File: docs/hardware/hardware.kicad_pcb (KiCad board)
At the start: 2 copper layers, 1.4 x 13 mm, 8 parts, among them J1 BASYS_JA, J2 AudioJack2, J6 BASYS_JB, J7 GAMEPAD_1, J8 GAMEPAD_2

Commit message: WIP ppu testing
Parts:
- A1: moved to B.Cu
- moved A1 48.3 mm to (53.3, 66.0)
- moved J7 33.0 mm to (30.5, 20.3)
- moved J8 30.5 mm to (30.5, 53.3)
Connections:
- J1 pad 1: SPI_CLK -> PPU_VRAM_WEN
- J1 pad 3: PPU_VRAM_WEN -> SPI_CLK
- J1 pad 5: (no net) -> GND
- J6 pad 5: unconnected-(J6-Pin_5-Pad5) -> GND
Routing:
- net PPU_VRAM_WEN: track 36.2 -> 26.0 mm
- net SPI_MOSI: track 46.3 -> 36.2 mm
- net SPI_CLK: track 54.0 -> 43.8 mm
- net GND: track 86.9 -> 90.0 mm

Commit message: finalize hardware
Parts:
- added J3: GAMEPAD, Connector_PinHeader_2.54mm:PinHeader_2x04_P2.54mm_Vertical, F.Cu at (119.4, 35.0)
- added SW1: LEFT, Button_Switch_THT:SW_PUSH_6mm, F.Cu at (79.9, 45.7)
- added SW2: UP, Button_Switch_THT:SW_PUSH_6mm, F.Cu at (90.8, 37.1)
- added SW3: RIGHT, Button_Switch_THT:SW_PUSH_6mm, F.Cu at (100.9, 45.7)
- added SW4: PRIMARY, Button_Switch_THT:SW_PUSH_6mm, F.Cu at (137.2, 45.7)
- added SW5: SECONDARY, Button_Switch_THT:SW_PUSH_6mm, F.Cu at (124.5, 45.7)
- added SW6: DOWN, Button_Switch_THT:SW_PUSH_6mm, F.Cu at (90.7, 54.6)
- moved C1 45.8 mm to (99.1, 81.4)
- moved J6 45.8 mm to (83.8, 78.7)
- moved R1 45.8 mm to (91.4, 78.7)
- moved J2 45.8 mm to (109.3, 83.7)
- moved J1 38.9 mm to (38.1, 27.9), turned to -90 degrees
- moved J8 29.0 mm to (58.4, 61.0), turned to 180 degrees
- moved A1 25.4 mm to (27.9, 66.0)
- moved J7 20.5 mm to (50.8, 22.9)
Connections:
- A1 pad 10: GP_P2_DOWN -> GP_P2_BUT_2
- A1 pad 11: GP_P2_LEFT -> GP_P2_BUT_1
- A1 pad 12: GP_P2_RIGHT -> GP_P2_LEFT
- A1 pad 13: GP_P2_BUT_1 -> GP_P2_UP
- A1 pad 14: GP_P2_BUT_2 -> GP_P2_RIGHT
- A1 pad 17: GP_P1_UP -> GP_P1_DOWN
- A1 pad 18: GP_P1_DOWN -> GP_P1_BUT_2
- A1 pad 19: GP_P1_LEFT -> GP_P1_BUT_1
- A1 pad 20: GP_P1_RIGHT -> GP_P1_LEFT
- A1 pad 21: GP_P1_BUT_1 -> GP_P1_UP
- A1 pad 22: GP_P1_BUT_2 -> GP_P1_RIGHT
- A1 pad 9: GP_P2_UP -> GP_P2_DOWN
- J7 pad 1: GP_P1_UP -> GP_P1_LEFT
- J7 pad 2: GP_P1_DOWN -> GP_P1_UP
- J7 pad 3: GP_P1_LEFT -> GP_P1_RIGHT
- J7 pad 5: GP_P1_RIGHT -> GP_P1_BUT_1
- J7 pad 6: GP_P1_BUT_1 -> GP_P1_BUT_2
- J7 pad 7: GP_P1_BUT_2 -> GP_P1_DOWN
- J8 pad 1: GP_P2_UP -> GP_P2_LEFT
- J8 pad 2: GP_P2_DOWN -> GP_P2_UP
- J8 pad 3: GP_P2_LEFT -> GP_P2_RIGHT
- J8 pad 5: GP_P2_RIGHT -> GP_P2_BUT_1
- J8 pad 6: GP_P2_BUT_1 -> GP_P2_BUT_2
- J8 pad 7: GP_P2_BUT_2 -> GP_P2_DOWN
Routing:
- net Net-(J3-VCC): track 0.00 -> 127.5 mm
- net Net-(J3-UP): track 0.00 -> 60.4 mm
- net VCC: track 0.00 -> 58.4 mm
- net GND: track 90.0 -> 49.4 mm, vias 0 -> 1
- net Net-(J3-SECONDARY): track 0.00 -> 39.6 mm
- net Net-(J3-RIGHT): track 0.00 -> 32.5 mm
- net Net-(J3-DOWN): track 0.00 -> 32.2 mm
- net SPI_CLK: track 43.8 -> 13.3 mm, vias 0 -> 1
- net SPI_MOSI: track 36.2 -> 10.8 mm, vias 0 -> 1
- net Net-(J3-PRIMARY): track 0.00 -> 22.0 mm
- net Net-(J3-LEFT): track 0.00 -> 20.1 mm
- net GP_P2_DOWN: track 0.00 -> 15.2 mm
- net GP_P2_RIGHT: track 0.00 -> 15.2 mm
- net GP_P1_RIGHT: track 0.00 -> 15.2 mm
- net GP_P1_DOWN: track 0.00 -> 15.2 mm
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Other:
- board text added: "ARDUINO SHIELD (TOP VIEW)"
- board text added: "GAMEPAD LAYOUT/PINOUT"
- board text added: "PWM AUDIO OUTPUT LOW PASS FILTER"

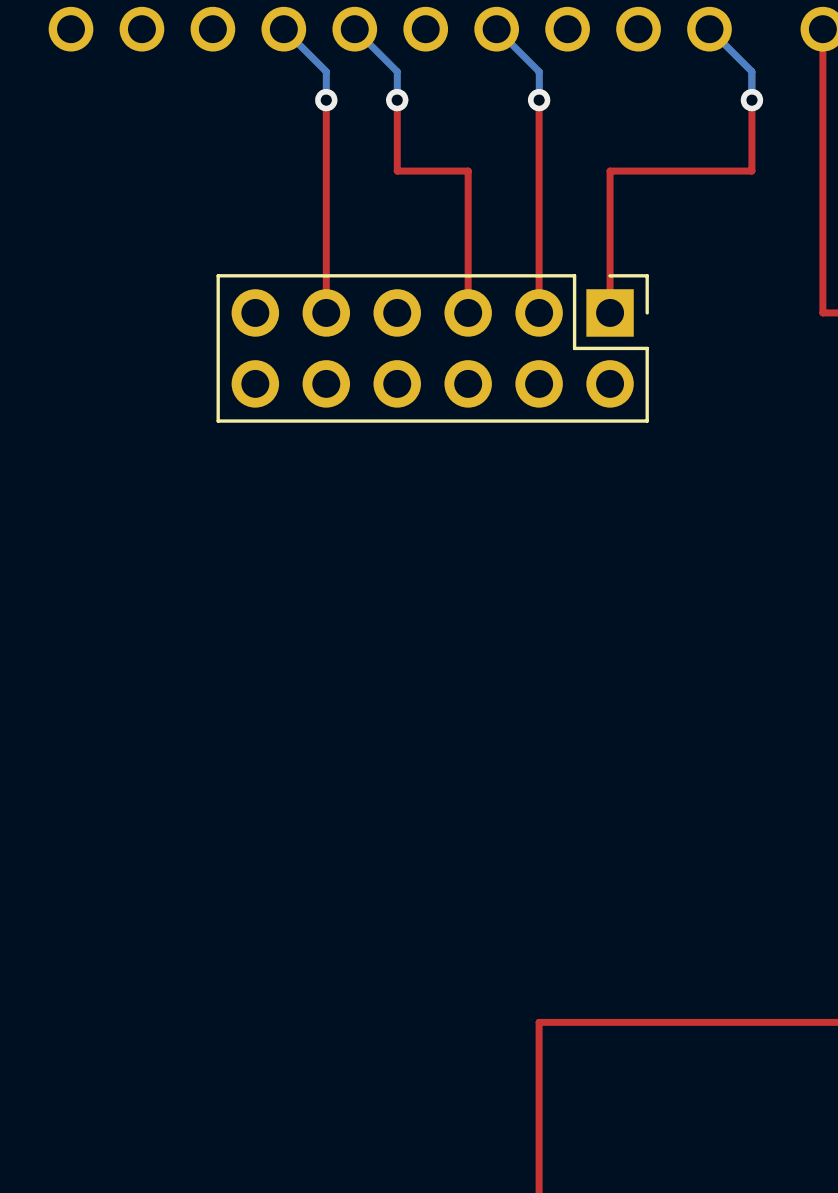
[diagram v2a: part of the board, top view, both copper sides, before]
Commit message: add power source toggle switch to hardware schematics
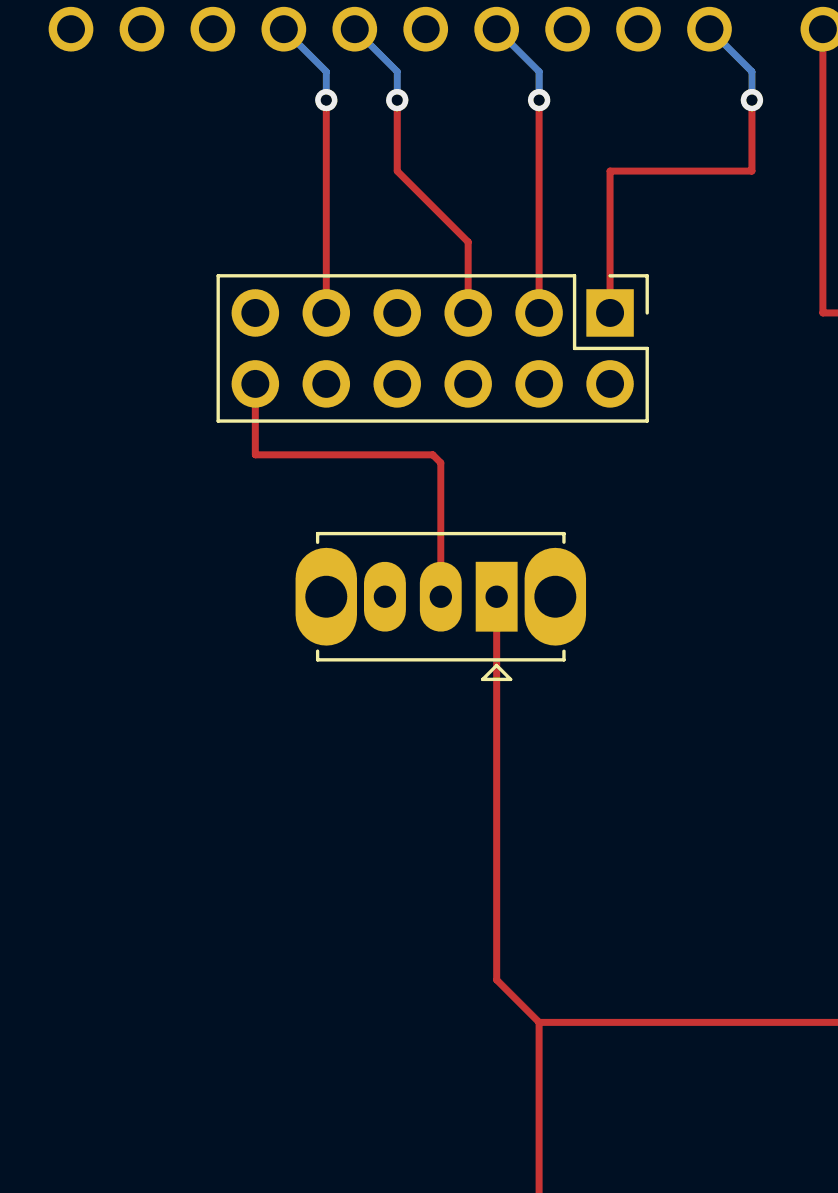
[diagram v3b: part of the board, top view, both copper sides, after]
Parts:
- added SW7: STM_PWR_SOURCE, Button_Switch_THT:SW_Slide_1P2T_CK_OS102011MS2Q, F.Cu at (34.0, 38.1)
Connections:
- J1 pad 12: unconnected-(J1-Pin_12-Pad12) -> Net-(J1-Pin_12)
- J1 pad 6: unconnected-(J1-Pin_6-Pad6) -> Net-(J1-Pin_12)
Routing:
- net VCC: track 58.4 -> 74.3 mm
- net Net-(J1-Pin_12): track 0.00 -> 14.1 mm
- net SPI_CLK: track 13.3 -> 11.8 mm
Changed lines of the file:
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@@
   (net 19 "Net-(C1-Pad1)")
   (net 20 "unconnected-(J1-Pin_4-Pad4)")
-  (net 21 "unconnected-(J1-Pin_6-Pad6)")
+  (net 21 "Net-(J1-Pin_12)")
   (net 22 "unconnected-(J1-Pin_7-Pad7)")
   (net 23 "unconnected-(J1-Pin_8-Pad8)")
   (net 24 "unconnected-(J1-Pin_9-Pad9)")
   (net 25 "unconnected-(J1-Pin_10-Pad10)")
-  (net 26 "unconnected-(J1-Pin_12-Pad12)")
+  (net 26 "unconnected-(SW7-C-Pad3)")
   (net 27 "unconnected-(J6-Pin_1-Pad1)")
   (net 28 "unconnected-(J6-Pin_2-Pad2)")
@@
         (effects (font (size 1 1) (thickness 0.15)))
     )
-    (fp_text value "BASYS_JA" (at 1.27 15.03 90) (layer "F.Fab")
+    (fp_text value "BASYS_JA" (at 1.27 15.03 90) (layer "F.Fab") hide
         (effects (font (size 1 1) (thickness 0.15)))
     )
@@
       (net 6 "GND") (pinfunction "Pin_5") (pintype "passive"))
     (pad "6" thru_hole oval (at 0 12.7 270) (size 1.7 1.7) (drill 1) (layers "*.Cu" "*.Mask")
-      (net 21 "unconnected-(J1-Pin_6-Pad6)") (pinfunction "Pin_6") (pintype "passive"))
+      (net 21 "Net-(J1-Pin_12)") (pinfunction "Pin_6") (pintype "passive"))
     (pad "7" thru_hole oval (at 2.54 0 270) (size 1.7 1.7) (drill 1) (layers "*.Cu" "*.Mask")
       (net 22 "unconnected-(J1-Pin_7-Pad7)") (pinfunction "Pin_7") (pintype "passive"))
@@
       (net 6 "GND") (pinfunction "Pin_11") (pintype "passive"))
     (pad "12" thru_hole oval (at 2.54 12.7 270) (size 1.7 1.7) (drill 1) (layers "*.Cu" "*.Mask")
-      (net 26 "unconnected-(J1-Pin_12-Pad12)") (pinfunction "Pin_12") (pintype "passive"))
+      (net 21 "Net-(J1-Pin_12)") (pinfunction "Pin_12") (pintype "passive"))
     (model "${KICAD6_3DMODEL_DIR}/Connector_PinHeader_2.54mm.3dshapes/PinHeader_2x06_P2.54mm_Vertical.wrl"
       (offset (xyz 0 0 0))
@@
         (effects (font (size 1 1) (thickness 0.15)))
     )
-    (fp_text value "GAMEPAD_2" (at 1.27 9.95) (layer "F.Fab")
-        (effects (font (size 1 1) (thickness 0.15)))
-    )
-    (fp_text user "${REFERENCE}" (at 1.27 3.81 90) (layer "F.Fab")
+    (fp_text value "GAMEPAD_2" (at 1.27 9.95) (layer "F.Fab") hide
         (effects (font (size 1 1) (thickness 0.15)))
     )
@@
       (net 40 "Net-(J3-VCC)") (pinfunction "B") (pintype "passive"))
     (model "${KICAD6_3DMODEL_DIR}/Button_Switch_THT.3dshapes/SW_PUSH_6mm.wrl"
+      (offset (xyz 0 0 0))
+      (scale (xyz 1 1 1))
+      (rotate (xyz 0 0 0))
+    )
+  )
+  (footprint "Button_Switch_THT:SW_Slide_1P2T_CK_OS102011MS2Q" (layer "F.Cu")
+    (at 34.04 38.1 180)
+    (descr "CuK miniature slide switch, OS series, SPDT, https://www.ckswitches.com/media/1428/os.pdf")
+    (tags "switch SPDT")
+    (property "Sheetfile" "hardware.kicad_sch")
+    (property "Sheetname" "")
+    (property "ki_description" "Switch, single pole double throw")
+    (property "ki_keywords" "switch single-pole double-throw spdt ON-ON")
+    (attr through_hole)
+    (fp_text reference "SW7" (at 3.99 -2.99) (layer "F.SilkS") hide
+        (effects (font (size 1 1) (thickness 0.15)))
+    )
+    (fp_text value "STM_PWR_SOURCE" (at 1.779337 -3.676307) (layer "F.Fab") hide
+        (effects (font (size 1 1) (thickness 0.15)))
+    )
+    (fp_line (start -2.41 -2.26) (end 6.41 -2.26)
+      (stroke (width 0.12) (type solid)) (layer "F.SilkS"))
+    (fp_line (start -2.41 -1.95) (end -2.41 -2.26)
+      (stroke (width 0.12) (type solid)) (layer "F.SilkS"))
+    (fp_line (start -2.41 2.26) (end -2.41 1.95)
+      (stroke (width 0.12) (type solid)) (layer "F.SilkS"))
+    (fp_line (start -0.5 -2.96) (end 0 -2.46)
+      (stroke (width 0.12) (type solid)) (layer "F.SilkS"))
+    (fp_line (start 0 -2.46) (end 0.5 -2.96)
+      (stroke (width 0.12) (type solid)) (layer "F.SilkS"))
+    (fp_line (start 0.5 -2.96) (end -0.5 -2.96)
+      (stroke (width 0.12) (type solid)) (layer "F.SilkS"))
+    (fp_line (start 6.41 -2.26) (end 6.41 -1.95)
+      (stroke (width 0.12) (type solid)) (layer "F.SilkS"))
+    (fp_line (start 6.41 2.26) (end -2.41 2.26)
+      (stroke (width 0.12) (type solid)) (layer "F.SilkS"))
+    (fp_line (start 6.41 2.26) (end 6.41 1.95)
+      (stroke (width 0.12) (type solid)) (layer "F.SilkS"))
+    (fp_line (start -3.45 -2.4) (end 7.45 -2.4)
+      (stroke (width 0.05) (type solid)) (layer "B.CrtYd"))
+    (fp_line (start -3.45 2.4) (end -3.45 -2.4)
+      (stroke (width 0.05) (type solid)) (layer "B.CrtYd"))
+    (fp_line (start 7.45 -2.4) (end 7.45 2.4)
+      (stroke (width 0.05) (type solid)) (layer "B.CrtYd"))
+    (fp_line (start 7.45 2.4) (end -3.45 2.4)
+      (stroke (width 0.05) (type solid)) (layer "B.CrtYd"))
+    (fp_line (start -2.3 -2.15) (end -0.5 -2.15)
+      (stroke (width 0.1) (type solid)) (layer "F.Fab"))
+    (fp_line (start -2.3 2.15) (end -2.3 -2.15)
+      (stroke (width 0.1) (type solid)) (layer "F.Fab"))
+    (fp_line (start -0.5 -2.15) (end 0 -1.65)
+      (stroke (width 0.1) (type solid)) (layer "F.Fab"))
+    (fp_line (start 0 -1.65) (end 0.5 -2.15)
+      (stroke (width 0.1) (type solid)) (layer "F.Fab"))
+    (fp_line (start 0 -1) (end 0 1)
+      (stroke (width 0.1) (type solid)) (layer "F.Fab"))
+    (fp_line (start 0 -1) (end 4 -1)
+      (stroke (width 0.1) (type solid)) (layer "F.Fab"))
+    (fp_line (start 0 1) (end 4 1)
+      (stroke (width 0.1) (type solid)) (layer "F.Fab"))
+    (fp_line (start 0.5 -2.15) (end 6.3 -2.15)
+      (stroke (width 0.1) (type solid)) (layer "F.Fab"))
+    (fp_line (start 0.66 -1) (end 0.66 1)
+      (stroke (width 0.1) (type solid)) (layer "F.Fab"))
+    (fp_line (start 1.34 -1) (end 1.34 1)
+      (stroke (width 0.1) (type solid)) (layer "F.Fab"))
+    (fp_line (start 2 -1) (end 2 1)
+      (stroke (width 0.1) (type solid)) (layer "F.Fab"))
+    (fp_line (start 4 -1) (end 4 1)
+      (stroke (width 0.1) (type solid)) (layer "F.Fab"))
+    (fp_line (start 6.3 -2.15) (end 6.3 2.15)
+      (stroke (width 0.1) (type solid)) (layer "F.Fab"))
+    (fp_line (start 6.3 2.15) (end -2.3 2.15)
+      (stroke (width 0.1) (type solid)) (layer "F.Fab"))
+    (pad "" thru_hole oval (at -2.1 0 180) (size 2.2 3.5) (drill 1.5) (layers "*.Cu" "*.Mask"))
+    (pad "" thru_hole oval (at 6.1 0 180) (size 2.2 3.5) (drill 1.5) (layers "*.Cu" "*.Mask"))
+    (pad "1" thru_hole rect (at 0 0 180) (size 1.5 2.5) (drill 0.8) (layers "*.Cu" "*.Mask")
+      (net 4 "VCC") (pinfunction "A") (pintype "passive"))
+    (pad "2" thru_hole oval (at 2 0 180) (size 1.5 2.5) (drill 0.8) (layers "*.Cu" "*.Mask")
+      (net 21 "Net-(J1-Pin_12)") (pinfunction "B") (pintype "passive"))
+    (pad "3" thru_hole oval (at 4 0 180) (size 1.5 2.5) (drill 0.8) (layers "*.Cu" "*.Mask")
+      (net 26 "unconnected-(SW7-C-Pad3)") (pinfunction "C") (pintype "passive+no_connect"))
+    (model "${KICAD6_3DMODEL_DIR}/Button_Switch_THT.3dshapes/SW_Slide_1P2T_CK_OS102011MS2Q.wrl"
       (offset (xyz 0 0 0))
       (scale (xyz 1 1 1))
@@
     )
   )
-  (gr_text "ARDUINO SHIELD\n(TOP VIEW)" (at 35.56 43.18) (layer "Dwgs.User")
+  (gr_text "ARDUINO SHIELD\n(TOP VIEW)" (at 22.86 58.42) (layer "Dwgs.User")
     (effects (font (size 1.5 1.5) (thickness 0.3) bold))
   )
@@
   (segment (start 50.8 53.34) (end 58.42 53.34) (width 0.25) (layer "F.Cu") (net 4))
   (segment (start 50.8 30.48) (end 50.8 53.34) (width 0.25) (layer "F.Cu") (net 4))
+  (segment (start 34.04 51.82) (end 35.56 53.34) (width 0.25) (layer "F.Cu") (net 4))
   (segment (start 50.8 53.34) (end 35.56 53.34) (width 0.25) (layer "F.Cu") (net 4))
+  (segment (start 34.04 38.1) (end 34.04 51.82) (width 0.25) (layer "F.Cu") (net 4))
   (segment (start 35.56 53.34) (end 35.56 66.04) (width 0.25) (layer "F.Cu") (net 4))
   (segment (start 111.76 83.82) (end 109.22 86.36) (width 0.25) (layer "F.Cu") (net 6))
@@
   (segment (start 35.56 19.3) (end 35.56 20.32) (width 0.25) (layer "B.Cu") (net 13))
   (segment (start 34.04 17.78) (end 35.56 19.3) (width 0.25) (layer "B.Cu") (net 13))
-  (segment (start 33.02 22.86) (end 33.02 27.94) (width 0.25) (layer "F.Cu") (net 15))
-  (segment (start 30.48 22.86) (end 33.02 22.86) (width 0.25) (layer "F.Cu") (net 15))
+  (segment (start 30.48 22.86) (end 33.02 25.4) (width 0.25) (layer "F.Cu") (net 15))
   (segment (start 30.48 20.32) (end 30.48 22.86) (width 0.25) (layer "F.Cu") (net 15))
+  (segment (start 33.02 25.4) (end 33.02 27.94) (width 0.25) (layer "F.Cu") (net 15))
   (via (at 30.48 20.32) (size 0.8) (drill 0.4) (layers "F.Cu" "B.Cu") (net 15))
   (segment (start 30.48 19.3) (end 30.48 20.32) (width 0.25) (layer "B.Cu") (net 15))
@@
   (segment (start 106.88 81.36) (end 109.26 83.74) (width 0.25) (layer "F.Cu") (net 19))
   (segment (start 99.06 81.36) (end 106.88 81.36) (width 0.25) (layer "F.Cu") (net 19))
+  (segment (start 31.753802 33.02) (end 32.04 33.306198) (width 0.25) (layer "F.Cu") (net 21))
+  (segment (start 32.04 33.306198) (end 32.04 38.1) (width 0.25) (layer "F.Cu") (net 21))
+  (segment (start 25.4 30.48) (end 25.4 33.02) (width 0.25) (layer "F.Cu") (net 21))
+  (segment (start 25.4 33.02) (end 31.753802 33.02) (width 0.25) (layer "F.Cu") (net 21))
   (segment (start 86.36 78.74) (end 91.44 78.74) (width 0.25) (layer "F.Cu") (net 32))
   (segment (start 86.36 29.9) (end 86.36 45.72) (width 0.25) (layer "F.Cu") (net 37))

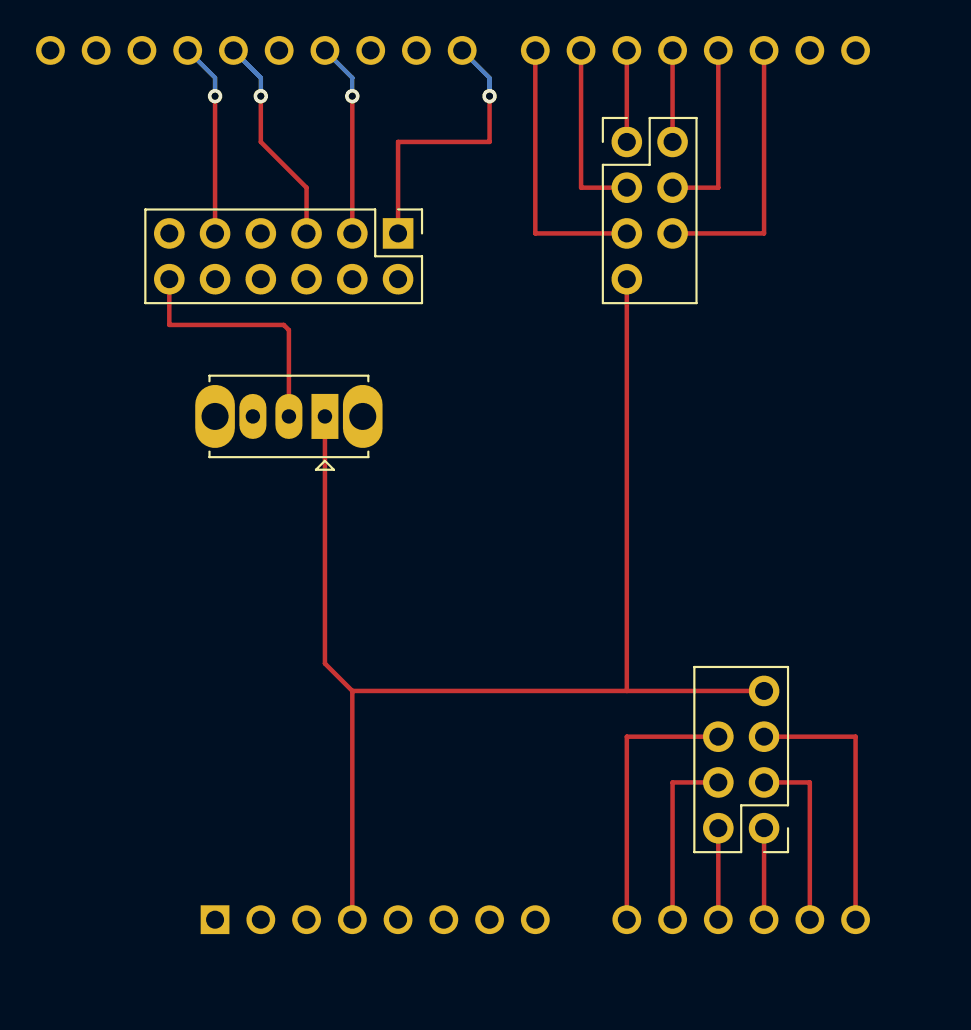
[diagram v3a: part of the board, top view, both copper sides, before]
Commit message: connect remaining ppu lines to stm
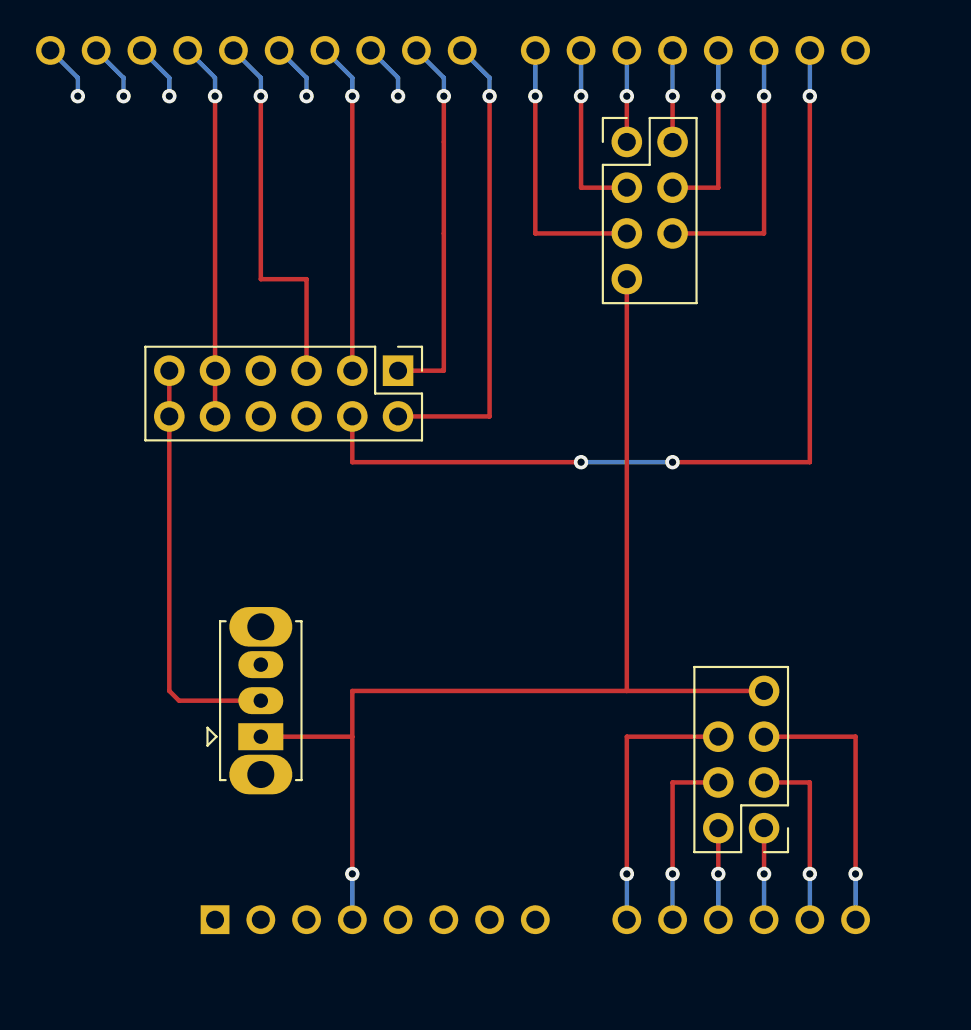
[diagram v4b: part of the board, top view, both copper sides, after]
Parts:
- moved SW7 18.1 mm to (30.5, 55.9), turned to 90 degrees
- moved J1 7.62 mm to (38.1, 35.6)
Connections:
- A1 pad 16: unconnected-(A1-D1/TX-Pad16) -> PPU_HBLANK
- A1 pad 23: PPU_VRAM_WEN -> SPI_SR
- A1 pad 24: unconnected-(A1-D9-Pad24) -> PPU_VBLANK
- J1 pad 1: PPU_VRAM_WEN -> PPU_VBLANK
- J1 pad 7: unconnected-(J1-Pin_7-Pad7) -> SPI_SR
- J1 pad 8: unconnected-(J1-Pin_8-Pad8) -> PPU_HBLANK
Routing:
- net PPU_HBLANK: track 0.00 -> 50.8 mm, vias 0 -> 3
- net SPI_SR: track 0.00 -> 26.0 mm, vias 0 -> 1
- net PPU_VBLANK: track 0.00 -> 20.9 mm, vias 0 -> 1
- net PPU_VRAM_WEN: track 15.9 -> 0.00 mm, vias 1 -> 0
- net VCC: track 74.3 -> 63.5 mm, vias 0 -> 1
- net GND: track 49.4 -> 59.5 mm
- net SPI_CLK: track 11.8 -> 20.9 mm
- net Net-(J1-Pin_12): track 14.1 -> 23.1 mm
- net SPI_MOSI: track 10.8 -> 18.4 mm
- net unconnected-(A1-D12-Pad27): track 0.00 -> 3.17 mm, vias 0 -> 1
- net unconnected-(A1-D10-Pad25): track 0.00 -> 3.17 mm, vias 0 -> 1
- net unconnected-(A1-SDA/A4-Pad31): track 0.00 -> 3.17 mm, vias 0 -> 1
- net unconnected-(A1-SCL/A5-Pad32): track 0.00 -> 3.17 mm, vias 0 -> 1
- net unconnected-(A1-AREF-Pad30): track 0.00 -> 3.17 mm, vias 0 -> 1
- net GP_P2_UP: vias 0 -> 1
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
